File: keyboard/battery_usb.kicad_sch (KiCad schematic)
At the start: 6 parts, among them SW1 SW_DIP_x01, U2 USB2514-HZH (C184347), U3 TPS62140

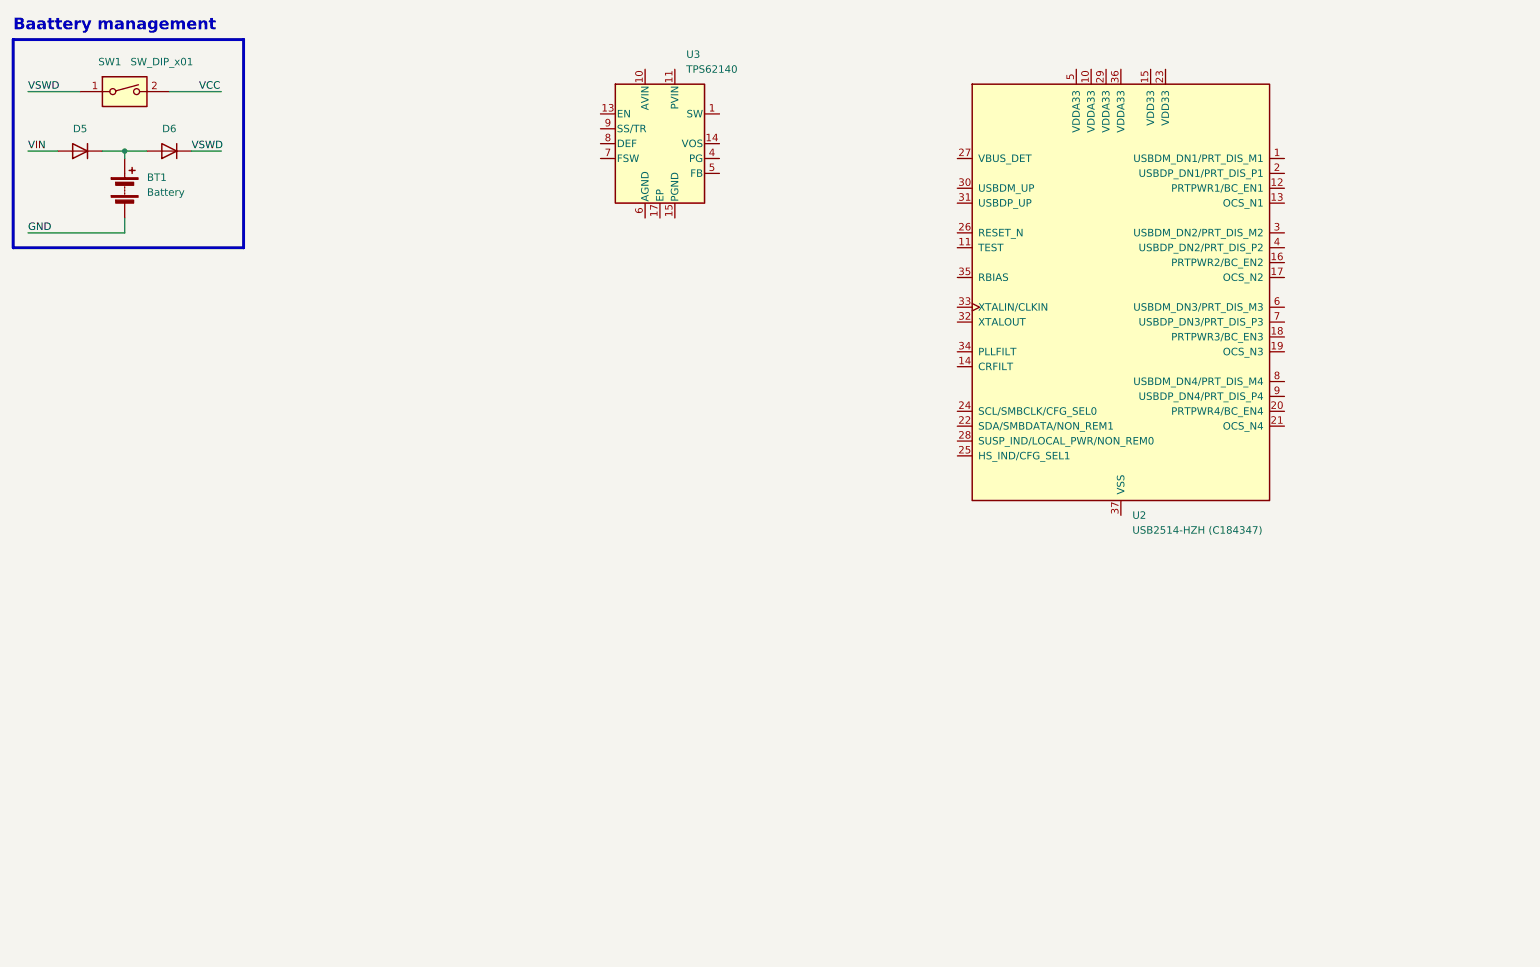
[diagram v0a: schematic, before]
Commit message: Added 3.3V
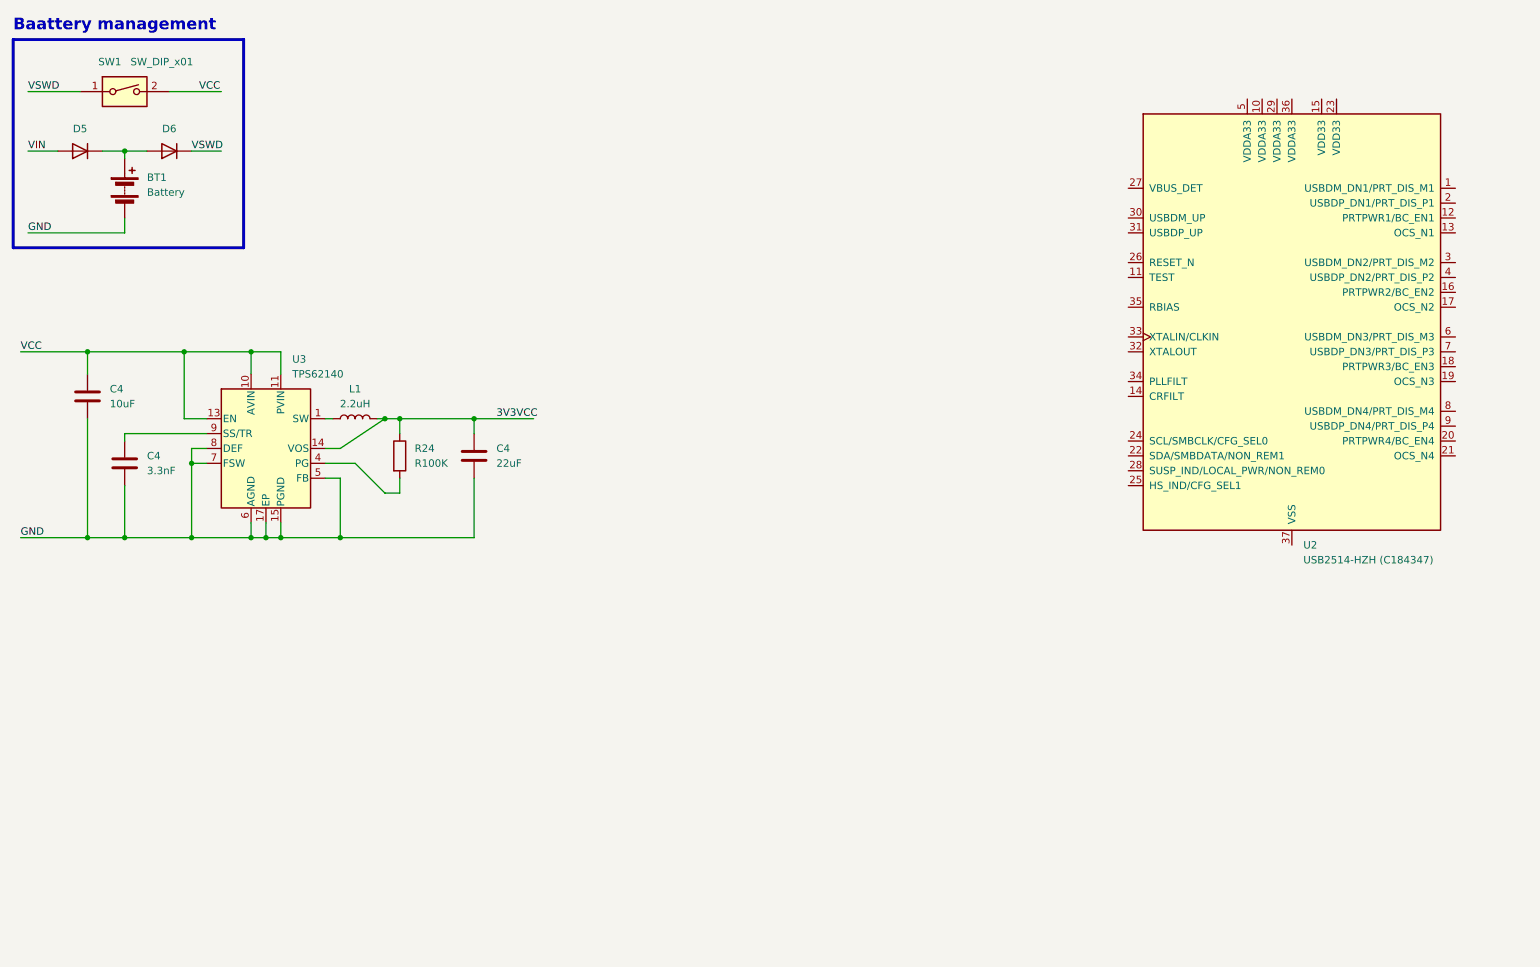
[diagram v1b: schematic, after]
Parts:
- added C4: 3.3nF, Capacitor_SMD:C_0402_1005Metric, symbol Device:C
- added C4: 10uF, Capacitor_SMD:C_0402_1005Metric, symbol Device:C
- added C4: 22uF, Capacitor_SMD:C_0402_1005Metric, symbol Device:C
- added L1: 2.2uH, symbol Device:L
- added R24: R100K, symbol Device:R
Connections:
- net GND: now also U3.15 (PGND), U3.16 (PGND), U3.17 (EP), U3.5 (FB), U3.6 (AGND), U3.7 (FSW), U3.8 (DEF), C4.2, C4.2, C4.2
- net VCC: now also U3.10 (AVIN), U3.11 (PVIN), U3.12 (PVIN), U3.13 (EN), C4.1
- net at U3.1 (SW), U3.2 (SW), U3.3 (SW): now also L1.1
- net 3V3VCC: now reaches U3.14 (VOS)
- net 3V3VCC: now also C4.1, L1.2, R24.1
- net at U3.4 (PG): now also R24.2
- net at U3.9 (SS/TR): now also C4.1
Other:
- moved on the sheet: U2, U3

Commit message: wireing
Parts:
- added C1 (x2): 1uF, Capacitor_SMD:C_0402_1005Metric, symbol Device:C
- added C3 (x2): 22pF, Capacitor_SMD:C_0402_1005Metric, symbol Device:C
- added R25: R12K, symbol Device:R
- added Y1: 48mhz, Crystal:Crystal_SMD_TXC_7M-4Pin_3.2x2.5mm, symbol Device:Crystal_GND24
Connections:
- net 3V3VCC: now also U2.10 (VDDA33), U2.15 (VDD33), U2.23 (VDD33), U2.27 (VBUS_DET), U2.29 (VDDA33), U2.36 (VDDA33), U2.5 (VDDA33)
- net GND: now also U2.37 (VSS), C1.2, C1.2, C3.2, C3.2, R25.1, Y1.2, Y1.4
- net USBMCU_D-: now reaches U2.1 (USBDM_DN1/PRT_DIS_M1)
- net at U2.14 (CRFILT): now also C1.1
- net USBMCU_D+: now reaches U2.2 (USBDP_DN1/PRT_DIS_P1)
- net RESET: now reaches U2.26 (RESET_N)
- net USBIN_D-: now reaches U2.30 (USBDM_UP)
- net USBIN_D+: now reaches U2.31 (USBDP_UP)
- net at U2.32 (XTALOUT): now also C3.1, Y1.3
- net at U2.33 (XTALIN/CLKIN): now also C3.1, Y1.1
- net at U2.34 (PLLFILT): now also C1.1
- net at U2.35 (RBIAS): now also R25.2
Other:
- moved on the sheet: U2

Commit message: usb hub wireing half
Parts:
- added R26, R27, R28, R29, R30, R31: R10K, symbol Device:R
- U2: footprint Package_DFN_QFN:VQFN-48-1EP_7x7mm_P0.5mm_EP4.1x4.1mm -> Package_DFN_QFN:VQFN-48-1EP_7x7mm_P0.5mm_EP4.1x4.1mm_ThermalVias
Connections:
- net 3V3VCC: now also U2.18 (VDD33), U2.30 (VDD33), U2.35 (VBUS_DET), U2.41 (VDD33), U2.48 (VDD33), R26.1, R31.1; no longer U2.15 (VDD33), U2.23 (VDD33), U2.27 (VBUS_DET), U2.29 (VDDA33), U2.36 (VDDA33)
- net GND: now also U2.49 (VSS), R27.1, R28.1, R29.1, R30.1; no longer U2.37 (VSS)
- net RESET: now also U2.34 (RESET_N); no longer U2.26 (RESET_N)
- net USBIN_D+: now also U2.43 (USBDP_UP); no longer U2.31 (USBDP_UP)
- net USBIN_D-: now also U2.42 (USBDM_UP); no longer U2.30 (USBDM_UP)
- net at U2.14 (TEST): no longer C1.1
- net at U2.17 (CRFILT): now also C1.1
- net USBHUBC1_D-: now reaches U2.3 (USBDM_DN2/PRT_DIS_M2)
- net at C3.1, Y1.3: now also U2.44 (XTALOUT); no longer U2.32 (XTALOUT)
- net at C3.1, Y1.1: now also U2.45 (XTALIN/CLKIN); no longer U2.33 (XTALIN/CLKIN)
- net at C1.1: now also U2.46 (PLLFILT); no longer U2.34 (PLLFILT)
- net at R25.2: now also U2.47 (RBIAS); no longer U2.35 (RBIAS)
- net USBHUBC1_D+: now reaches U2.4 (USBDP_DN2/PRT_DIS_P2)
- net USBHUBA1_D-: now reaches U2.6 (USBDM_DN3/PRT_DIS_M3)
- net USBHUBA1_D+: now reaches U2.7 (USBDP_DN3/PRT_DIS_P3)
- net USBHUBA2_D-: now reaches U2.8 (USBDM_DN4/PRT_DIS_M4)
- net USBHUBA2_D+: now reaches U2.9 (USBDP_DN4/PRT_DIS_P4)
- new net CFG_SEL0: R29.2, U2.31 (SCL/SMBCLK/CFG_SEL0)
- new net CFG_SEL1: R28.2, U2.32 (HS_IND/CFG_SEL1)
- new net CFG_SEL2: R27.2, U2.33 (CFG_SEL2)
- new net NON_REM0: R31.2, U2.39 (SUSP_IND/LOCAL_PWR/NON_REM0)
- new net NON_REM1: R30.2, U2.29 (SDA/SMBDATA/NON_REM1)
- new net SEL48: R26.2, U2.40 (SEL48)
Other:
- moved on the sheet: BT1, C1, C3, C4, D5, D6, L1, R24, R25, SW1, U3, Y1
